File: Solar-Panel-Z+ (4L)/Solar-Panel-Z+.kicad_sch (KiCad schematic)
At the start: 73 parts, among them J1 FTS-105-01-L-DV-A, Q1 BSS138DWQ-7, Q2 MBT2222ADW1T1, Q3 BSS138DWQ-7, Q4 MBT2222ADW1T1, U1 BQ25570RGRR, U2 TSL2561

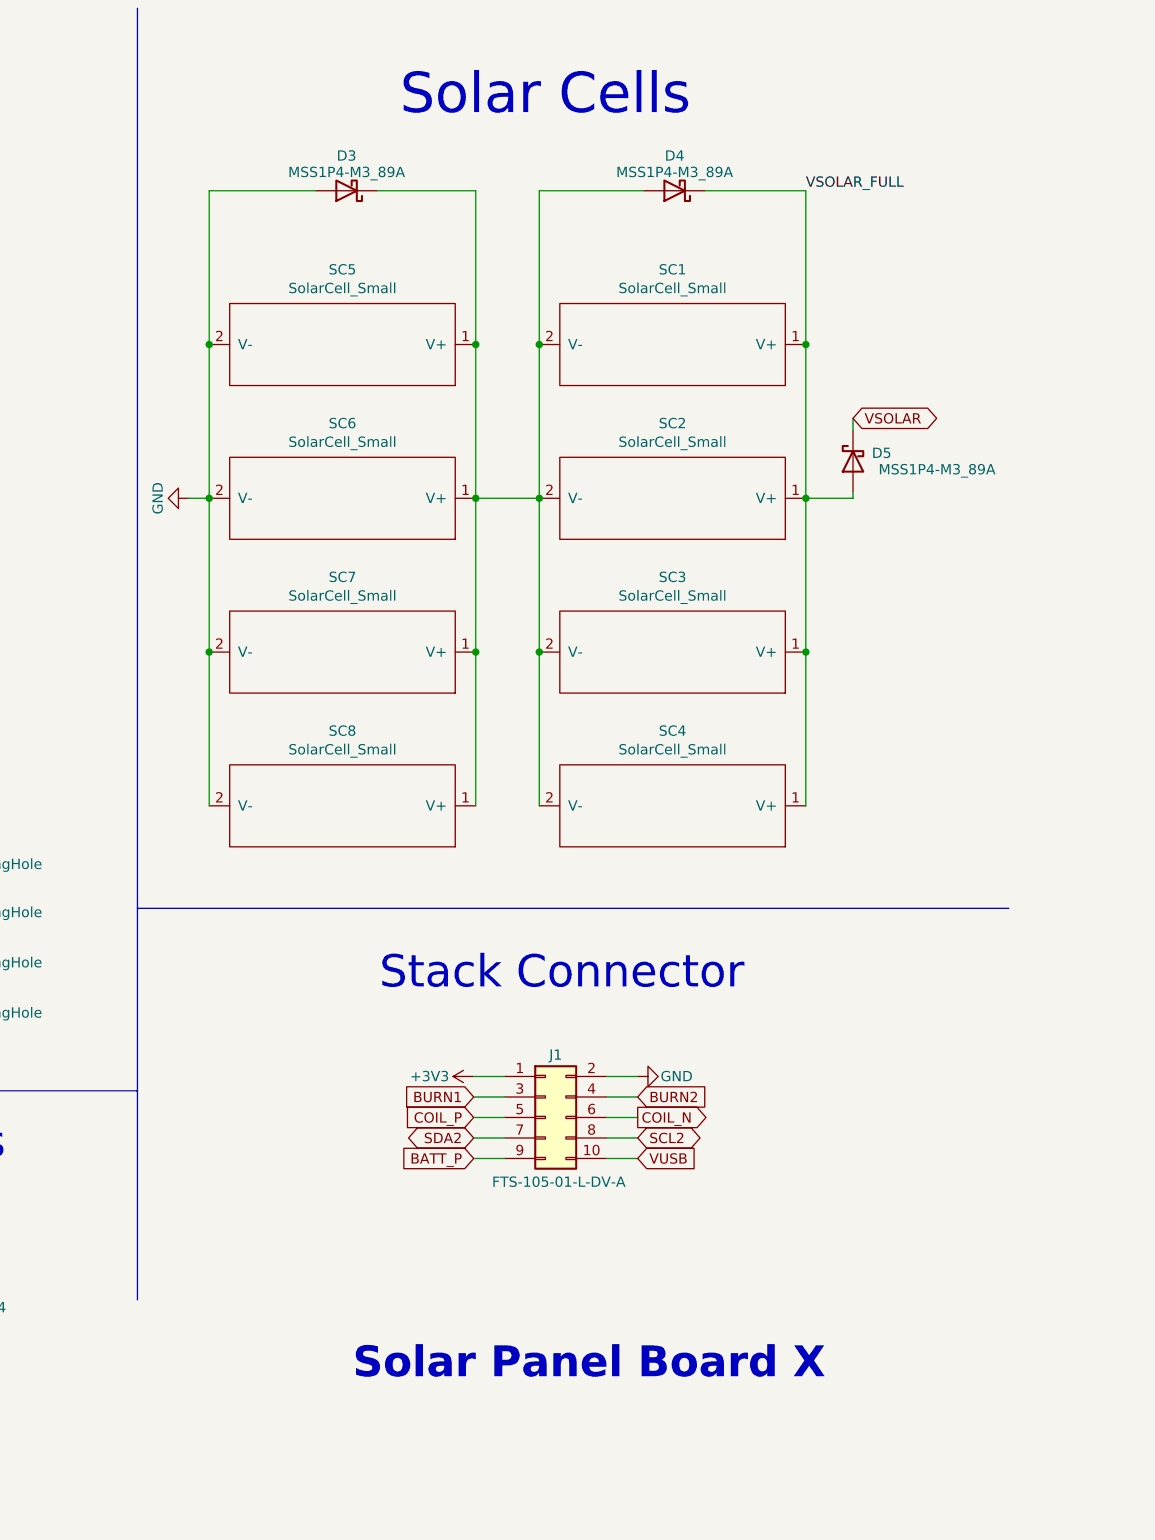
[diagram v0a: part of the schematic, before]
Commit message: Added 4 Layer Z+ board
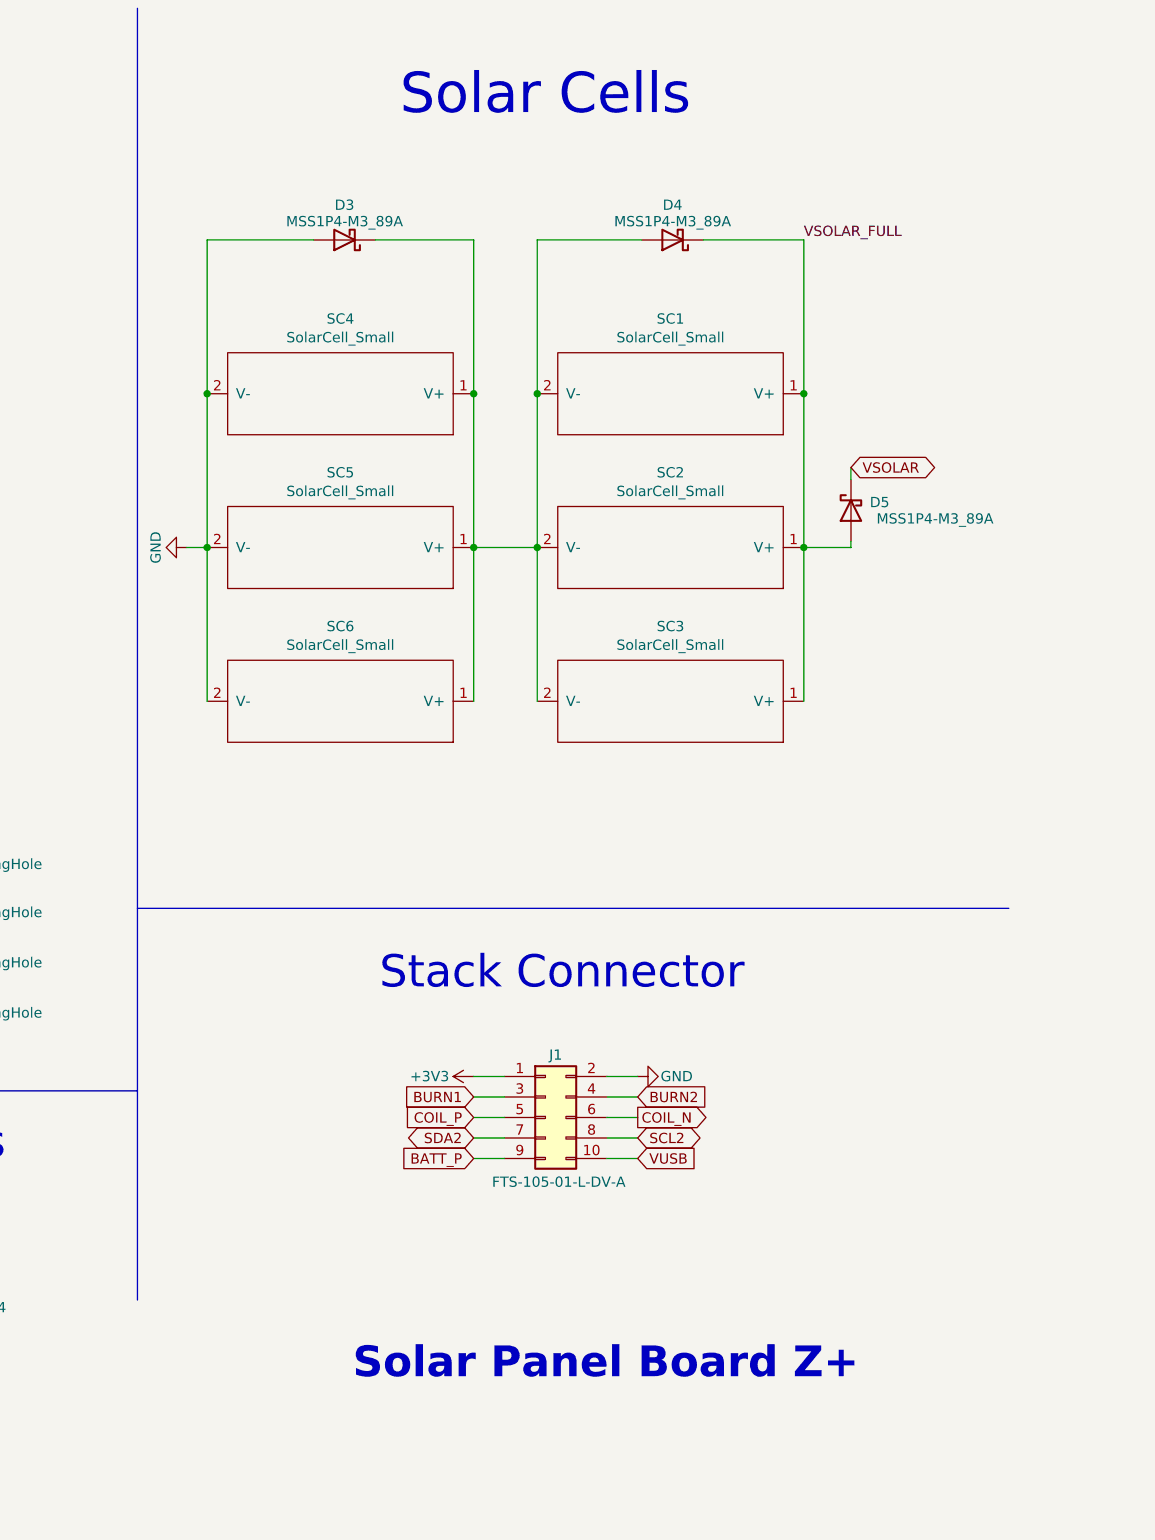
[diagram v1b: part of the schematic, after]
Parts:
- removed SC4, SC8: SolarCell_Small, solarpanels:KXOB25-05X3F, symbol solarpanels:SolarCell_Small
- renumbered SC5 to SC4, SC6 to SC5, SC7 to SC6
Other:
- note added: "Solar Panel Board Z+"
- note removed: "Solar Panel Board X"
- moved on the sheet: D3, D4, D5, SC1, SC2, SC3, SC4, SC5, SC6

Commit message: Updated all solar panels to Rev B2/01 + Export STEP / BOM
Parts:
- C10, C11, C12, C13, C2, C3, C4, C6, C7, C8, C9: footprint Capacitor_SMD:C_0402_1005Metric -> Capacitor_SMD:C_0603_1608Metric
- J1: footprint batteryboard:FTS-105-XX-YY-DV-A -> solarpanels:SAMTEC-FTS-105-01-X-DV-A
- R10, R11, R12, R13, R16, R17, R18, R3, R5, R6, R7, R8, R9: footprint Resistor_SMD:R_0402_1005Metric -> Resistor_SMD:R_0603_1608Metric
- R14, R15: value 0 -> DNI; footprint Resistor_SMD:R_0402_1005Metric -> Resistor_SMD:R_0603_1608Metric
- R19: renamed from R22; value 0 -> DNI; footprint Resistor_SMD:R_0402_1005Metric -> Resistor_SMD:R_0603_1608Metric
- R20: renamed from R23; value 0 -> DNI; footprint Resistor_SMD:R_0402_1005Metric -> Resistor_SMD:R_0603_1608Metric
- R21: renamed from R20; footprint Resistor_SMD:R_0402_1005Metric -> Resistor_SMD:R_0603_1608Metric
- R22: renamed from R21; footprint Resistor_SMD:R_0402_1005Metric -> Resistor_SMD:R_0603_1608Metric
- R23: renamed from R24; footprint Resistor_SMD:R_0402_1005Metric -> Resistor_SMD:R_0603_1608Metric
- R24: renamed from R25; footprint Resistor_SMD:R_0402_1005Metric -> Resistor_SMD:R_0603_1608Metric
- R25: renamed from R26; footprint Resistor_SMD:R_0402_1005Metric -> Resistor_SMD:R_0603_1608Metric
- R26: renamed from R27; footprint Resistor_SMD:R_0402_1005Metric -> Resistor_SMD:R_0603_1608Metric
- R27: renamed from R28; footprint Resistor_SMD:R_0402_1005Metric -> Resistor_SMD:R_0603_1608Metric
- R28: renamed from R29; footprint Resistor_SMD:R_0402_1005Metric -> Resistor_SMD:R_0603_1608Metric
- R29: renamed from R30; footprint Resistor_SMD:R_0402_1005Metric -> Resistor_SMD:R_0603_1608Metric
- R30: renamed from R31; footprint Resistor_SMD:R_0402_1005Metric -> Resistor_SMD:R_0603_1608Metric
- R4: renamed from R19; footprint Resistor_SMD:R_0402_1005Metric -> Resistor_SMD:R_0603_1608Metric
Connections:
- net BURN2 is gone; now on net GND: J1.4 (Pin_4)
- net VUSB is gone; now on net BATT_P: J1.10 (Pin_10)
- net SCL2 renamed SCL
- net SDA2 renamed SDA
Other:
- moved on the sheet: R20

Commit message: Changed TSL2591 to BH1750
All boards (4L) except -Y
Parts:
- removed U2: TSL2561, solarpanels:TSL2561, symbol solarpanels:symbols_TSL2561
- added U2: BH1750FVI-TR, WSOF6, symbol solarpanels:BH1750FVI-TR
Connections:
- net +3V3: now also U2.1 (VCC)
- net GND: now also U2.3 (GND)
- net SCL_LS: now also U2.6 (SCL)
- net SDA_LS: now also U2.4 (SDA)
- net at R10.2, R5.2, R7.2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: now also R5.1, R6.2, U1.7 (VBAT_OV)
- net at R1.1, R2.2: now also U2.2 (ADDR)
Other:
- moved on the sheet: C2, C3, C6, D1, D5, H1, H2, H3, H4, J1, R3, R4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

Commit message: Updated light sensor to OPT 3001, Updated solar diodes.
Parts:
- removed C12, C13: 10nF, Capacitor_SMD:C_0603_1608Metric, symbol Device:C
- removed D5: MSS1P4-M3_89A, solarpanels:MICROSMP, symbol Device:D_Schottky
- removed Q1, Q3: BSS138DWQ-7, Package_TO_SOT_SMD:SOT-363_SC-70-6, symbol mainboard:BSS138DWQ-7
- removed Q2, Q4: MBT2222ADW1T1, Package_TO_SOT_SMD:SOT-363_SC-70-6, symbol Transistor_BJT:MBT2222ADW1T1
- removed R19, R20: DNI, Resistor_SMD:R_0603_1608Metric, symbol Device:R_US
- removed R21, R26: 680, Resistor_SMD:R_0603_1608Metric, symbol Device:R_US
- removed R22, R27: 100K, Resistor_SMD:R_0603_1608Metric, symbol Device:R_US
- removed R23, R24, R28, R29: 10K, Resistor_SMD:R_0603_1608Metric, symbol Device:R_US
- removed R25, R30: 200K, Resistor_SMD:R_0603_1608Metric, symbol Device:R_US
- removed U2: BH1750FVI-TR, WSOF6, symbol solarpanels:BH1750FVI-TR
- added U2: OPT3001, solarpanels:OPT3001, symbol solarpanels:OPT3001
- added U3: MAX40200AUK, Package_TO_SOT_SMD:SOT-23-5, symbol Analog_Switch:MAX40200AUK
- D2, D3, D4: value MSS1P4-M3_89A -> DFLS130L-7; footprint solarpanels:MICROSMP -> Diode_SMD:D_PowerDI-123; Allied Price/Stock https://www.alliedelec.com/general-semiconductor-vishay-mss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 -> (none); Allied_Number 70217632 -> (none); Manufacturer_Name Vishay -> (none); Manufacturer_Part_Number MSS1P4-M3/89A -> (none); Mouser Part Number 625-MSS1P4-M3 -> (none); Mouser Price/Stock https://www.mouser.com/Search/Refine.aspx?Keyword=625-MSS1P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 -> (none); RS Part Number 7103068P -> (none); RS Price/Stock http://uk.rs-online.com/web/p/products/7103068P -> (none)
- J1: value FTS-105-01-L-DV-A -> FTS-105-01-X-DV-A
- R1, R12, R13, R16, R17, R18, R2, R3, R4: value 0 -> 0R
- R14, R15: value DNI -> DNI (0R)
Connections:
- net +3V3: now also U2.1 (VDD), U3.5 (OUT); no longer D2.1 (K)
- net GND: now also U2.3 (GND), U2.7 (GND), U3.2 (GND)
- net SCL_LS: now also U2.4 (SCL)
- net SDA_LS: now also U2.6 (SDA)
- net VSOLAR: now also D2.1 (K)
- net VSOLAR_FULL: now also D2.2 (A)
- net at R10.2, R5.2, R7.2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: no longer R5.1, R6.2, U1.7 (VBAT_OV)
- net at R1.1, R2.2: now also U2.2 (ADDR)
- net at C10.1, C8.1, L2.2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: now also U3.1 (VDD), U3.3 (EN); no longer D2.2 (A)
- new net: R5.1, R6.2, U1.7 (VBAT_OV)
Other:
- added sheet Bus Protection (BusProtection.kicad_sch)
- note added: "Populate R1 for I2C addr 0x45, OR Populate R2 for I2C addr 0x44"
- note added: "To Mainboard"
- note removed: "I2C Bus Protection - Light Sensor"
- moved on the sheet: C1, C11, R1, R12, R13, R17, R18, R2, R7, R9

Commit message: B3/02 Updates
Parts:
- C1: value 1uF -> 0.1uF
- H1, H2, H3, H4: footprint MountingHole:MountingHole_2.2mm_M2_DIN965_Pad -> solarpanels:MountingHole_2.2mm_M2_DIN965_Pad_TopBottom; now left out of the parts list
- TP1, TP2, TP3, TP4: now left out of the parts list
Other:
- moved on the sheet: C1, R1, R2, U2

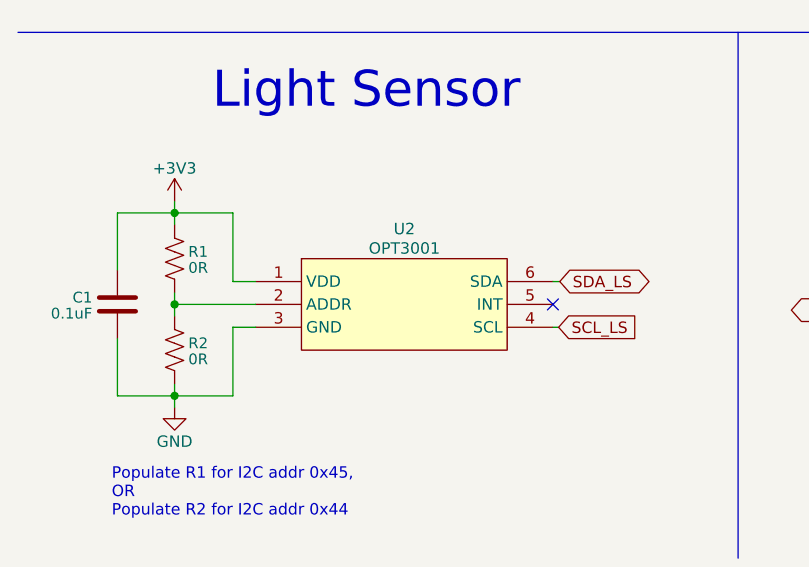
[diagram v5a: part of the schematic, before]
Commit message: Updated Sun Sensor to OPT4001
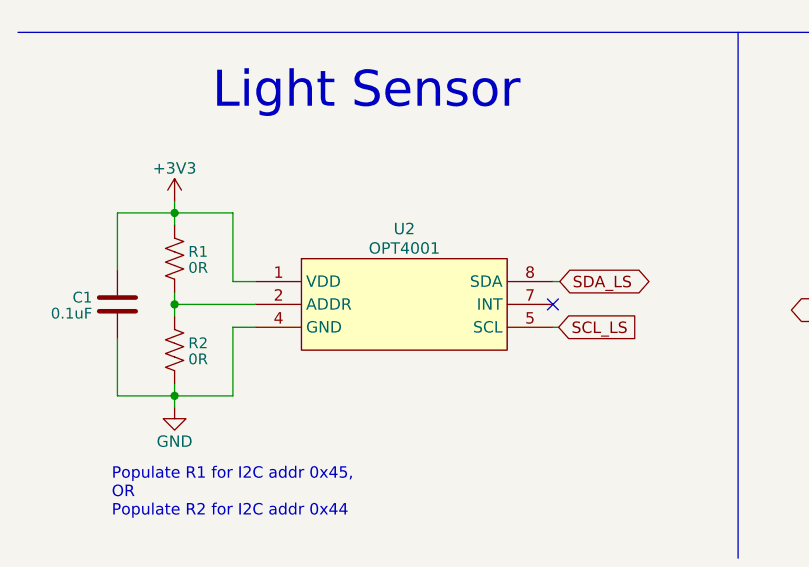
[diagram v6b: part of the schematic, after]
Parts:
- U2: value OPT3001 -> OPT4001; footprint solarpanels:OPT3001 -> Package_TO_SOT_SMD:SOT-583-8; symbol solarpanels:OPT3001 -> solarpanels:OPT4001
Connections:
- net GND: now also U2.4 (GND); no longer U2.3 (GND), U2.7 (GND)
- net SCL_LS: now also U2.5 (SCL); no longer U2.4 (SCL)
- net SDA_LS: now also U2.8 (SDA); no longer U2.6 (SDA)
- new net: U2.3 (NC), U2.6 (NC)
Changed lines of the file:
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@@
     )
   )
-  (symbol (lib_id "solarpanels:OPT3001") (at 54.356 176.276 0) (unit 1)
+  (symbol (lib_id "solarpanels:OPT4001") (at 54.356 176.276 0) (unit 1)
     (in_bom yes) (on_board yes) (dnp no)
     (property "Reference" "U2" (at 54.356 167.894 0)
       (effects (font (size 1.27 1.27)))
     )
-    (property "Value" "OPT3001" (at 54.356 170.053 0)
+    (property "Value" "OPT4001" (at 54.356 170.053 0)
       (effects (font (size 1.27 1.27)))
     )
-    (property "Footprint" "solarpanels:OPT3001" (at 54.356 182.626 0)
+    (property "Footprint" "Package_TO_SOT_SMD:SOT-583-8" (at 54.356 182.626 0)
       (effects (font (size 1.27 1.27)) hide)
     )
@@
     (pin "6")
     (pin "7")
+    (pin "8")
     (instances
       (project "Solar-Panel-Z+"
